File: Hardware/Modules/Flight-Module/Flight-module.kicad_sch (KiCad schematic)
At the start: 27 parts, among them J3 Conn_01x01_Pin, J4 B6B-EH-A, J5 B6B-EH-A, J6 Conn_01x01_Pin, J7 Conn_01x01_Pin, U1 BMP390, U2 SAM-M10Q-00B, U3 PCA9306DCTR, U4 ICM-20948, U5 TLV70018_SOT23-5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

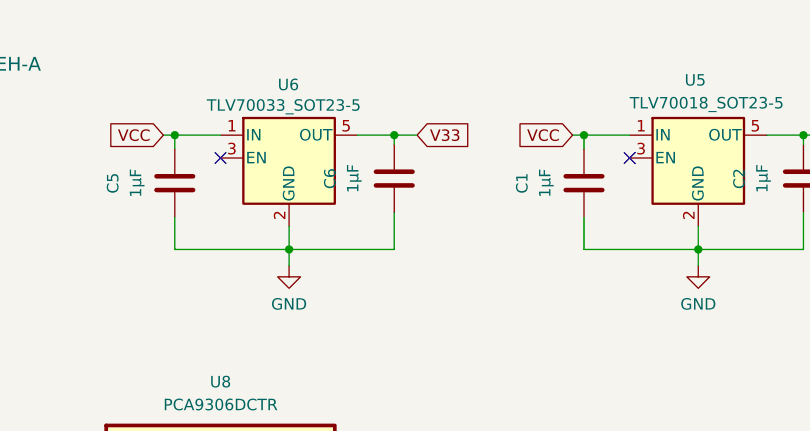
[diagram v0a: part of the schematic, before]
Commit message: Finishing Modules
Wifi-Module
Flight-Module
REPAIR:
- Heartrate
- Flight-Module
- Wifi-Module
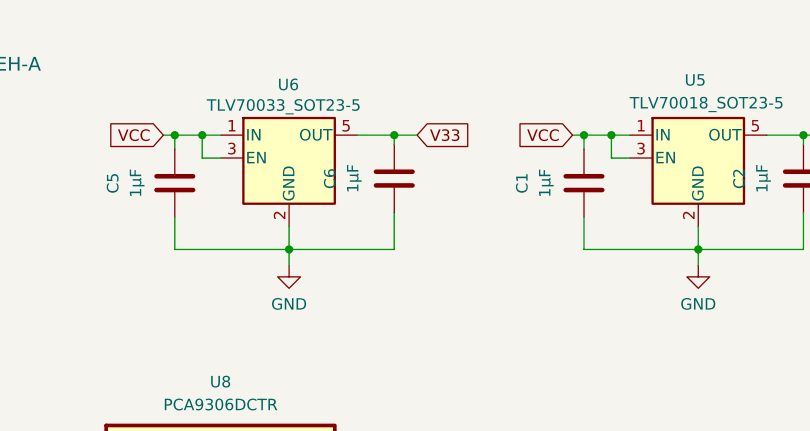
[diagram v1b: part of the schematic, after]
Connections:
- net VCC: now also U5.3 (EN), U6.3 (EN)
- no-connect marks 9 -> 7
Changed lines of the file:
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@@
+	)
+	(junction
+		(at 139.7 31.242)
+		(diameter 0)
+		(color 0 0 0 0)
+	)
+	(junction
+		(at 185.166 31.242)
+		(diameter 0)
+		(color 0 0 0 0)
 	)
 	(junction
@@
 	)
 	(no_connect
-		(at 141.732 33.782)
-	)
-	(no_connect
 		(at 181.864 114.808)
 	)
@@
 	)
 	(no_connect
-		(at 187.198 33.782)
-	)
-	(no_connect
 		(at 28.702 83.058)
 	)
@@
 	(wire
 		(pts
-			(xy 136.652 31.242) (xy 141.732 31.242)
+			(xy 136.652 31.242) (xy 139.7 31.242)
 		)
 		(stroke
@@
 	(wire
 		(pts
-			(xy 182.118 31.242) (xy 187.198 31.242)
+			(xy 182.118 31.242) (xy 185.166 31.242)
 		)
 		(stroke
@@
 	(wire
 		(pts
+			(xy 185.166 33.782) (xy 185.166 31.242)
+		)
+		(stroke
+			(width 0)
+			(type default)
+		)
+	)
+	(wire
+		(pts
+			(xy 187.198 33.782) (xy 185.166 33.782)
+		)
+		(stroke
+			(width 0)
+			(type default)
+		)
+	)
+	(wire
+		(pts
 			(xy 194.564 132.588) (xy 194.564 135.382)
 		)
@@
 	(wire
 		(pts
+			(xy 139.7 33.782) (xy 139.7 31.242)
+		)
+		(stroke
+			(width 0)
+			(type default)
+		)
+	)
+	(wire
+		(pts
 			(xy 117.348 71.12) (xy 123.952 71.12)
 		)
@@
 	(wire
 		(pts
+			(xy 185.166 31.242) (xy 187.198 31.242)
+		)
+		(stroke
+			(width 0)
+			(type default)
+		)
+	)
+	(wire
+		(pts
 			(xy 100.584 30.988) (xy 100.584 32.766)
 		)
@@
 	(wire
 		(pts
+			(xy 141.732 33.782) (xy 139.7 33.782)
+		)
+		(stroke
+			(width 0)
+			(type default)
+		)
+	)
+	(wire
+		(pts
 			(xy 92.202 111.76) (xy 93.218 111.76)
 		)
@@
 		)
 		(stroke
+			(width 0)
+			(type default)
+		)
+	)
+	(wire
+		(pts
+			(xy 139.7 31.242) (xy 141.732 31.242)
+		)
+		(stroke

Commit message: Pushing Final Versions of all Modules (2025)
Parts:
- U1: footprint Modular_Electronics_Toolkit_Footprints:10LGA_2X2X0p75_BOS -> Modular-Elektronics-Toolkit-Global-Libary:10LGA_2X2X0p75_BOS
- U2: footprint Modular_Electronics_Toolkit_Footprints:XCVR_SAM-M10Q-00B -> Modular-Elektronics-Toolkit-Global-Libary:XCVR_SAM-M10Q-00B
- U3, U7, U8: footprint Modular_Electronics_Toolkit_Footprints:SOP65P400X130-8N -> Modular-Elektronics-Toolkit-Global-Libary:SOP65P400X130-8N
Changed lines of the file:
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@@
 (kicad_sch
-	(version 20231120)
+	(version 20250114)
 	(generator "eeschema")
-	(generator_version "8.0")
+	(generator_version "9.0")
 	(paper "A4")
 	(junction
@@
 			)
 		)
-		(property "Footprint" "Modular_Electronics_Toolkit_Footprints:SOP65P400X130-8N"
+		(property "Footprint" "Modular-Elektronics-Toolkit-Global-Libary:SOP65P400X130-8N"
 			(at 112.776 143.51 0)
 			(effects
@@
 			)
 		)
-		(property "Footprint" "Modular_Electronics_Toolkit_Footprints:SOP65P400X130-8N"
+		(property "Footprint" "Modular-Elektronics-Toolkit-Global-Libary:SOP65P400X130-8N"
 			(at 141.986 58.166 0)
 			(effects
@@
 			)
 		)
-		(property "Footprint" "Modular_Electronics_Toolkit_Footprints:XCVR_SAM-M10Q-00B"
+		(property "Footprint" "Modular-Elektronics-Toolkit-Global-Libary:XCVR_SAM-M10Q-00B"
 			(at 51.562 56.896 0)
 			(effects
@@
 			)
 		)
-		(property "Footprint" "Modular_Electronics_Toolkit_Footprints:SOP65P400X130-8N"
+		(property "Footprint" "Modular-Elektronics-Toolkit-Global-Libary:SOP65P400X130-8N"
 			(at 254 70.866 0)
 			(effects
@@
 			)
 		)
-		(property "Footprint" "Modular_Electronics_Toolkit_Footprints:10LGA_2X2X0p75_BOS"
+		(property "Footprint" "Modular-Elektronics-Toolkit-Global-Libary:10LGA_2X2X0p75_BOS"
 			(at 114.808 108.712 0)
 			(effects
@@
 		)
 	)
+	(embedded_fonts no)
 )
